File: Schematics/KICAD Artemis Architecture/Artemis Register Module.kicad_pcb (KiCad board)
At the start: 4 copper layers, 56.5 x 36 mm, 24 parts, among them J1 Power, J2 Bus, J3 Control, J4 A Value, U4 74LS173, U5 74LS173, U6 74LS245

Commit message: Unhooked Project from OneDrive
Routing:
- net /A7: track 66.2 -> 83.0 mm
- net /BUS 0: track 65.3 -> 59.6 mm
- net GNDREF: track 24.9 -> 27.1 mm, vias 2 -> 1
- net VCC: track 76.0 -> 77.8 mm, vias 1 -> 0
- net /A4: track 67.5 -> 66.8 mm
- net /A5: track 67.2 -> 66.6 mm
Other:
- board text removed: "Current Value"
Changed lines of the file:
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@@
-		)
-	)
-	(gr_text "Current\nValue"
-		(at 126.6 92.8 0)
-		(layer "F.SilkS")
-		(effects
-			(font
-				(size 1 1)
-				(thickness 0.1)
-			)
-			(justify bottom)
 		)
 	)
@@
 		)
 	)
-	(gr_text "Bus"
-		(at 94.75 76.75 90)
-		(layer "F.SilkS")
-		(effects
-			(font
-				(size 1 1)
-				(thickness 0.1)
-			)
-			(justify left bottom)
-		)
-	)
 	(gr_text "R4"
 		(at 133.3 83.6 90)
@@
 		)
 	)
-	(gr_text "Power"
-		(at 94.75 67.25 90)
-		(layer "F.SilkS")
-		(effects
-			(font
-				(size 1 1)
-				(thickness 0.1)
-			)
-			(justify left bottom)
-		)
-	)
 	(gr_text "74LS173"
 		(at 108.75 67 0)
@@
 	)
 	(segment
+		(start 98.85 64.375)
+		(end 99.8 65.325)
+		(width 1)
+		(layer "F.Cu")
+		(net 2)
+	)
+	(segment
 		(start 126.5 84.1)
 		(end 129.6 84.1)
@@
 	)
 	(segment
-		(start 99.8 65.325)
-		(end 97.975 65.325)
-		(width 1)
-		(layer "F.Cu")
-		(net 2)
-	)
-	(segment
 		(start 120.3 84.1)
 		(end 123.4 84.1)
@@
 	)
 	(segment
-		(start 97.975 65.325)
-		(end 97.97 65.32)
+		(start 96.2 64.375)
+		(end 98.85 64.375)
 		(width 1)
 		(layer "F.Cu")
@@
 		(net 2)
 	)
-	(via
-		(at 97.97 65.32)
-		(size 0.6)
-		(drill 0.3)
-		(layers "F.Cu" "B.Cu")
-		(net 2)
-	)
 	(segment
 		(start 123.4 78.575)
@@
 	)
 	(segment
+		(start 125 73)
+		(end 116.14 73)
+		(width 0.5)
+		(layer "F.Cu")
+		(net 11)
+	)
+	(segment
+		(start 126.5 74.5)
+		(end 125 73)
+		(width 0.5)
+		(layer "F.Cu")
+		(net 11)
+	)
+	(segment
 		(start 116.14 73)
 		(end 113.44 70.3)
@@
 	)
 	(segment
-		(start 126 73)
-		(end 116.14 73)
-		(width 0.5)
-		(layer "F.Cu")
-		(net 11)
-	)
-	(segment
 		(start 126.5 75.6)
-		(end 126.5 73.5)
-		(width 0.5)
-		(layer "F.Cu")
-		(net 11)
-	)
-	(segment
-		(start 126.5 73.5)
-		(end 126 73)
+		(end 126.5 74.5)
 		(width 0.5)
 		(layer "F.Cu")
@@
 	)
 	(segment
-		(start 97.98 63.13)
-		(end 98.87 63.13)
+		(start 96.2 63.125)
+		(end 98.875 63.125)
 		(width 1)
 		(layer "F.Cu")
@@
 	)
 	(segment
-		(start 98.87 63.13)
+		(start 98.875 63.125)
 		(end 99.8 62.2)
 		(width 1)
 		(layer "F.Cu")
-		(net 12)
-	)
-	(via
-		(at 97.98 63.13)
-		(size 0.6)
-		(drill 0.3)
-		(layers "F.Cu" "B.Cu")
 		(net 12)
 	)
@@
 	)
 	(segment
+		(start 113.66 80.335)
+		(end 113.66 75.6)
+		(width 0.5)
+		(layer "F.Cu")
+		(net 13)
+	)
+	(segment
+		(start 122.225 88.9)
+		(end 113.66 80.335)
+		(width 0.5)
+		(layer "F.Cu")
+		(net 13)
+	)
+	(segment
 		(start 120.3 75.6)
 		(end 113.66 75.6)
@@
 	)
 	(segment
-		(start 135.8 73.38)
+		(start 135.8 75.6)
+		(end 135.8 74.3)
+		(width 0.5)
+		(layer "F.Cu")
+		(net 16)
+	)
+	(segment
+		(start 132.72 71.22)
 		(end 132.72 70.3)
 		(width 0.5)
@@
 	)
 	(segment
-		(start 135.8 75.6)
-		(end 135.8 73.38)
+		(start 135.8 74.3)
+		(end 132.72 71.22)
+		(width 0.5)
+		(layer "F.Cu")
+		(net 16)
+	)
+	(segment
+		(start 132.8 70.3)
+		(end 132.72 70.3)
 		(width 0.5)
 		(layer "F.Cu")
@@
 	)
 	(segment
-		(start 128.5 72)
-		(end 117.68 72)
-		(width 0.5)
-		(layer "F.Cu")
-		(net 17)
-	)
-	(segment
-		(start 129.6 75.6)
-		(end 129.6 73.1)
+		(start 129.6 74.35)
+		(end 127.25 72)
 		(width 0.5)
 		(layer "F.Cu")
@@
 	)
 	(segment
-		(start 129.6 73.1)
-		(end 128.5 72)
+		(start 127.25 72)
+		(end 117.68 72)
+		(width 0.5)
+		(layer "F.Cu")
+		(net 17)
+	)
+	(segment
+		(start 129.6 75.6)
+		(end 129.6 74.35)
 		(width 0.5)
 		(layer "F.Cu")
@@
 	)
 	(segment
+		(start 142 75.6)
+		(end 142 74.5)
+		(width 0.5)
+		(layer "F.Cu")
+		(net 21)
+	)
+	(segment
 		(start 142 74.5)
 		(end 137.8 70.3)
@@
 	)
 	(segment
-		(start 142 75.6)
-		(end 142 74.5)
-		(width 0.5)
-		(layer "F.Cu")
-		(net 21)
-	)
-	(segment
 		(start 130.975 88.9)
 		(end 130.975 88.475)
@@
 	)
 	(segment
+		(start 138.9 74.4)
+		(end 135.26 70.76)
+		(width 0.5)
+		(layer "F.Cu")
+		(net 22)
+	)
+	(segment
+		(start 135.26 70.3)
+		(end 135.3 70.3)
+		(width 0.5)
+		(layer "F.Cu")
+		(net 22)
+	)
+	(segment
 		(start 138.9 75.6)
-		(end 138.9 73.94)
+		(end 138.9 74.4)
 		(width 0.5)
 		(layer "F.Cu")
@@
 	)
 	(segment
-		(start 138.9 73.94)
+		(start 135.26 70.76)
 		(end 135.26 70.3)
 		(width 0.5)
@@
 	(segment
 		(start 132.7 75.6)
-		(end 132.7 72.82)
+		(end 132.7 74.2)
 		(width 0.5)
 		(layer "F.Cu")
@@
 	)
 	(segment
-		(start 132.7 72.82)
+		(start 132.7 74.2)
+		(end 130.18 71.68)
+		(width 0.5)
+		(layer "F.Cu")
+		(net 24)
+	)
+	(segment
+		(start 130.18 71.68)
 		(end 130.18 70.3)
 		(width 0.5)
@@
 	)
 	(segment
-		(start 96.75 80.425)
-		(end 96.2 79.875)
+		(start 110.855 79.875)
+		(end 115.78 84.8)
+		(width 0.5)
+		(layer "F.Cu")
+		(net 25)
+	)
+	(segment
+		(start 96.2 79.875)
+		(end 110.855 79.875)
+		(width 0.5)
+		(layer "F.Cu")
+		(net 25)
+	)
+	(segment
+		(start 139.05 63.93)
+		(end 137.8 62.68)
 		(width 0.5)
 		(layer "In2.Cu")
@@
 	)
 	(segment
-		(start 139.05 63.93)
-		(end 137.8 62.68)
+		(start 139.05 71.217767)
+		(end 139.05 63.93)
 		(width 0.5)
 		(layer "In2.Cu")
@@
 	)
 	(segment
-		(start 96.75 85.75)
-		(end 96.75 80.425)
-		(width 0.5)
-		(layer "In2.Cu")
-		(net 25)
-	)
-	(segment
-		(start 139.05 71.217767)
-		(end 139.05 63.93)
-		(width 0.5)
-		(layer "In2.Cu")
-		(net 25)
-	)
-	(segment
 		(start 115.78 84.8)
 		(end 125.467767 84.8)
 		(width 0.5)
 		(layer "In2.Cu")
-		(net 25)
-	)
-	(segment
-		(start 99 88)
-		(end 96.75 85.75)
-		(width 0.5)
-		(layer "In2.Cu")
-		(net 25)
-	)
-	(segment
-		(start 112.58 88)
-		(end 99 88)
-		(width 0.5)
-		(layer "In2.Cu")
-		(net 25)
-	)
-	(segment
-		(start 115.78 84.8)
-		(end 112.58 88)
-		(width 0.5)
-		(layer "In2.Cu")

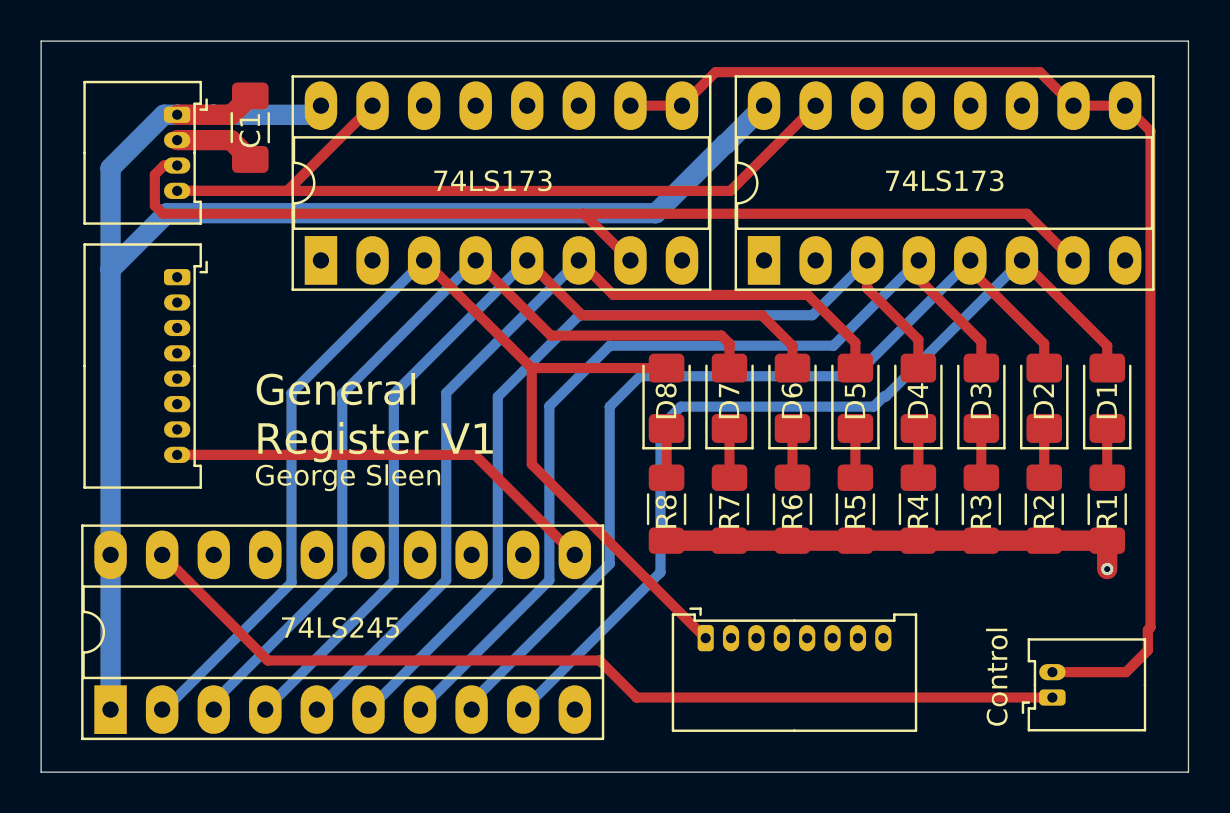
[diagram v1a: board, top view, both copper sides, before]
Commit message: Finished Register Silkscreen
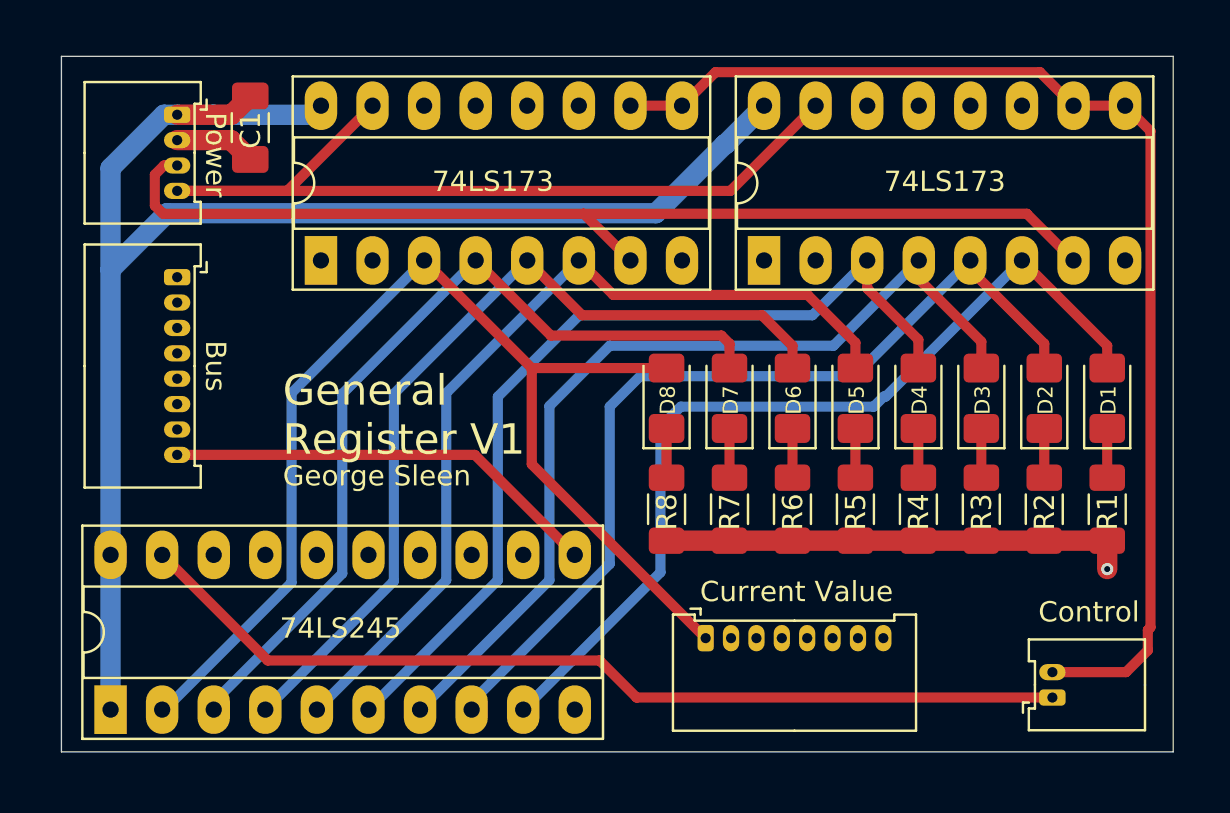
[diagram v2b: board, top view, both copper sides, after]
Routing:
- removed copper zone on In2.Cu, net (none)
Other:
- board size 56.5 x 36 mm -> 54.8 x 34.2 mm
- board text added: "Current Value"
